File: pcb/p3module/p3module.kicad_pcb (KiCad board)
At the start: 2 copper layers, 38 parts, among them J1 Conn_01x08_Female, J2 Conn_02x10_Counter_Clockwise, J3 Conn_01x08_Female, U1 74HC595, U2 74HC165, U3 74HC595, U4 4051

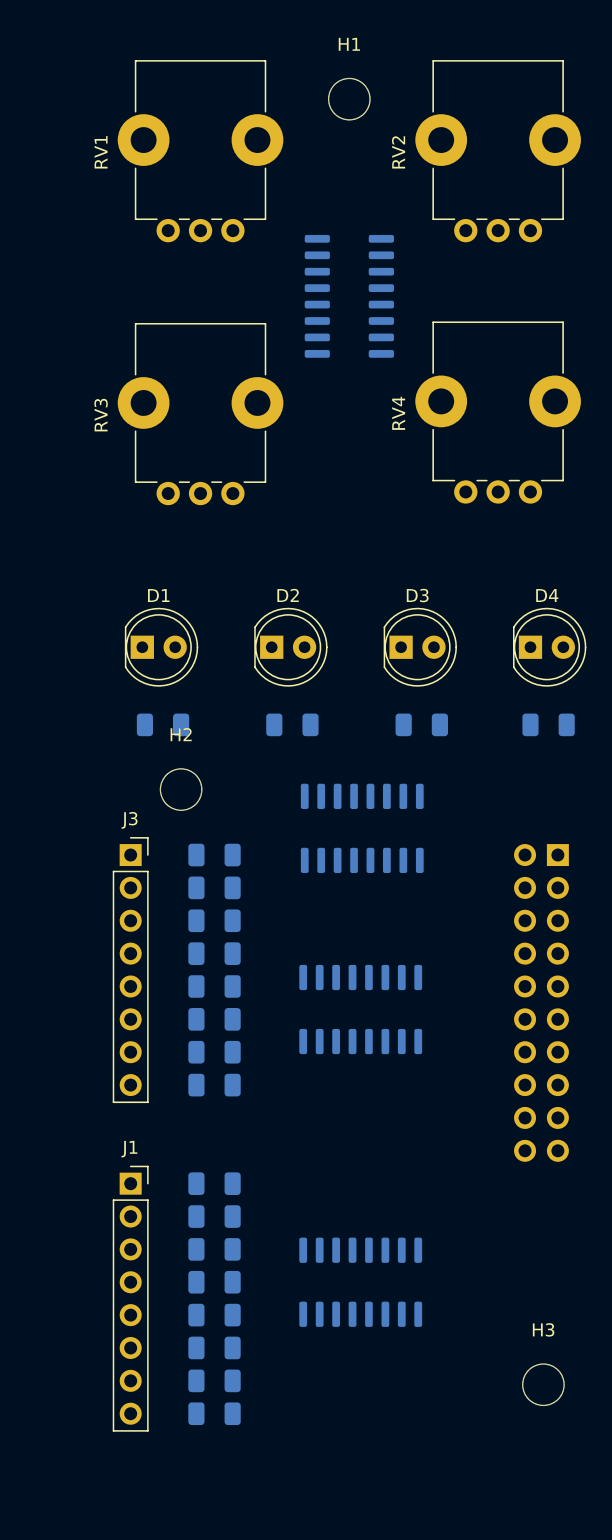
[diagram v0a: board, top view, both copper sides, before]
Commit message: reduced width to 6HP
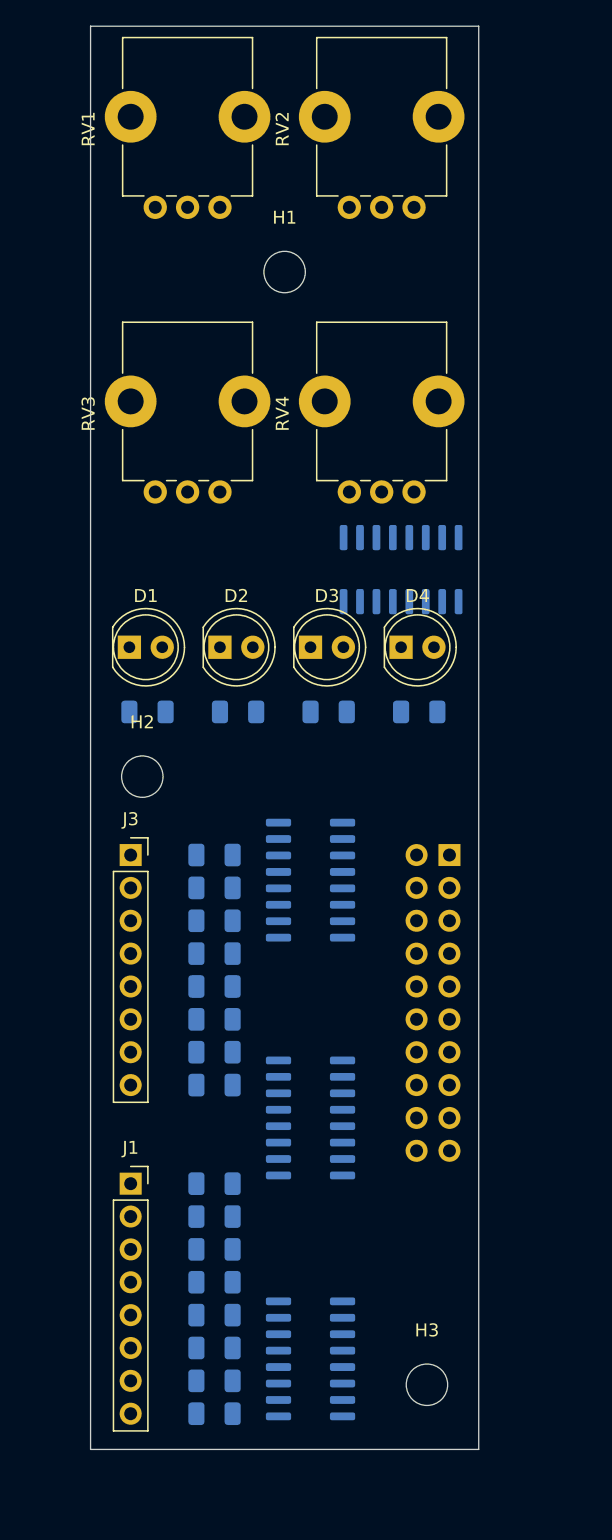
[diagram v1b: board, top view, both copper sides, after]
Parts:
- moved U4 21.5 mm to (59.0, 77.0), turned to 270 degrees
- moved H1 14.3 mm to (50.0, 54.0)
- moved R20 10.0 mm to (60.4, 88.0)
- moved D4 10.0 mm to (59.0, 83.0)
- moved U2 9.23 mm to (52.0, 119.4), turned to 180 degrees
- moved RV2 9.18 mm to (60.0, 49.0)
- moved H3 9.00 mm to (61.0, 140.0)
- moved RV4 9.00 mm to (60.0, 71.0)
- moved J2 8.38 mm to (62.7, 99.1)
- moved R19 7.27 mm to (53.4, 88.0)
- moved U1 7.08 mm to (52.0, 138.0), turned to 180 degrees
- moved D3 7.00 mm to (52.0, 83.0)
- moved U3 5.66 mm to (52.0, 101.0), turned to 180 degrees
- moved R18 4.32 mm to (46.4, 88.0)
- moved D2 4.00 mm to (45.0, 83.0)
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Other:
- board outline added: 30 x 110 mm

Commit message: reduced height to 10cm
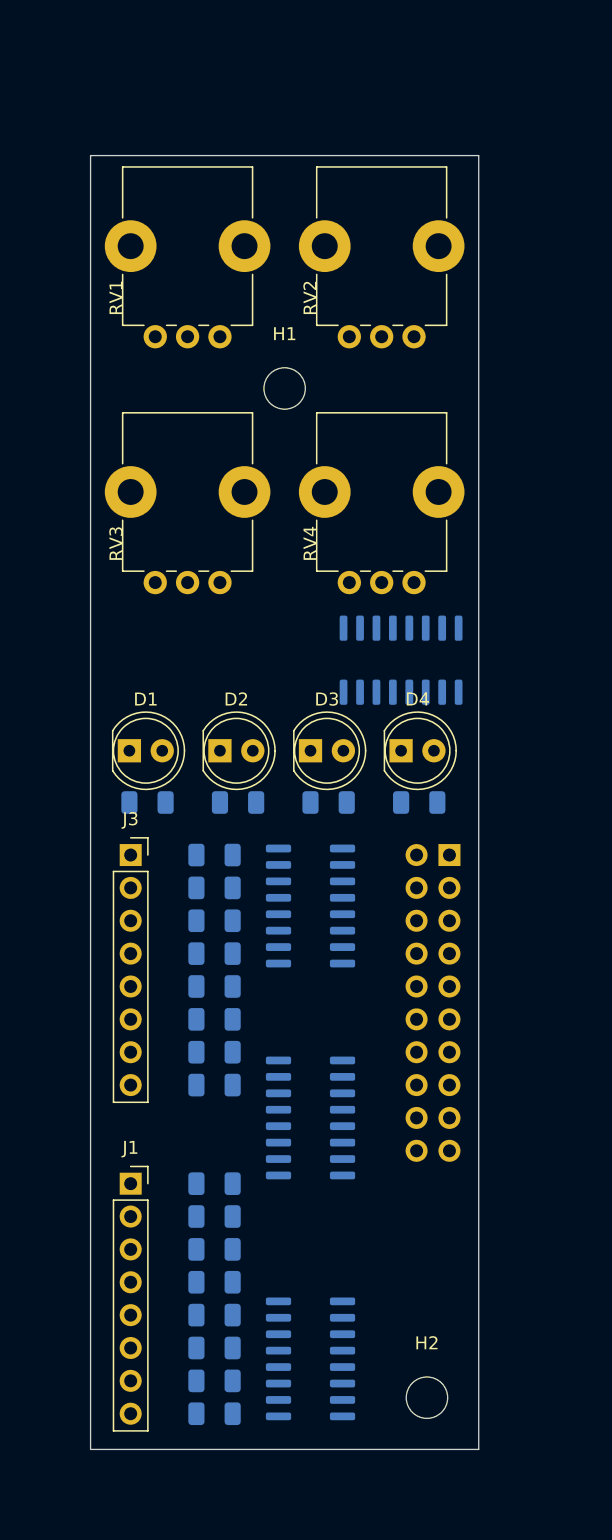
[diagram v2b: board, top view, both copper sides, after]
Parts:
- removed H3: MountingHole, MountingHole:MountingHole_3.2mm_M3
- moved H2 52.8 mm to (61.0, 141.0)
- moved RV1 10.0 mm to (45.0, 59.0)
- moved RV2 10.0 mm to (60.0, 59.0)
- moved H1 9.00 mm to (50.0, 63.0)
- moved D1 8.00 mm to (38.0, 91.0)
- moved D2 8.00 mm to (45.0, 91.0)
- moved D3 8.00 mm to (52.0, 91.0)
- moved D4 8.00 mm to (59.0, 91.0)
- moved R17 7.00 mm to (39.4, 95.0)
- moved R18 7.00 mm to (46.4, 95.0)
- moved R19 7.00 mm to (53.4, 95.0)
- moved R20 7.00 mm to (60.4, 95.0)
- moved RV3 7.00 mm to (45.0, 78.0)
- moved RV4 7.00 mm to (60.0, 78.0)
- moved U4 7.00 mm to (59.0, 84.0)
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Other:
- board size 30 x 110 mm -> 30 x 100 mm
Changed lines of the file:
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@@
   (general
     (thickness 1.6)
-    (drawings 8)
+    (drawings 4)
     (tracks 0)
     (zones 0)
-    (modules 38)
+    (modules 37)
     (nets 66)
   )
@@
   )
   (module Package_SO:SOIC-16_3.9x9.9mm_P1.27mm (layer B.Cu)
-    (at 59 77 270)
+    (at 59 84 270)
     (descr "SOIC, 16 Pin (JEDEC MS-012AC, https://www.analog.com/media/en/package-pcb-resources/package/pkg_pdf/soic_narrow-r/r_16.pdf), generated with kicad-footprint-generator ipc_gullwing_generator.py")
     (tags "SOIC SO")
@@
   )
   (module Package_SO:SOIC-16_3.9x9.9mm_P1.27mm (layer B.Cu)
-    (at 52 101 180)
+    (at 52 103 180)
     (descr "SOIC, 16 Pin (JEDEC MS-012AC, https://www.analog.com/media/en/package-pcb-resources/package/pkg_pdf/soic_narrow-r/r_16.pdf), generated with kicad-footprint-generator ipc_gullwing_generator.py")
     (tags "SOIC SO")
@@
   )
   (module Resistor_SMD:R_1206_3216Metric (layer B.Cu)
-    (at 60.4 88 180)
+    (at 60.4 95 180)
     (descr "Resistor SMD 1206 (3216 Metric), square (rectangular) end terminal, IPC_7351 nominal, (Body size source: http://www.tortai-tech.com/upload/download/2011102023233369053.pdf), generated with kicad-footprint-generator")
     (tags resistor)
@@
   )
   (module Resistor_SMD:R_1206_3216Metric (layer B.Cu)
-    (at 53.4 88 180)
+    (at 53.4 95 180)
     (descr "Resistor SMD 1206 (3216 Metric), square (rectangular) end terminal, IPC_7351 nominal, (Body size source: http://www.tortai-tech.com/upload/download/2011102023233369053.pdf), generated with kicad-footprint-generator")
     (tags resistor)
@@
   )
   (module Resistor_SMD:R_1206_3216Metric (layer B.Cu)
-    (at 46.4 88 180)
+    (at 46.4 95 180)
     (descr "Resistor SMD 1206 (3216 Metric), square (rectangular) end terminal, IPC_7351 nominal, (Body size source: http://www.tortai-tech.com/upload/download/2011102023233369053.pdf), generated with kicad-footprint-generator")
     (tags resistor)
@@
   )
   (module Resistor_SMD:R_1206_3216Metric (layer B.Cu)
-    (at 39.4 88 180)
+    (at 39.4 95 180)
     (descr "Resistor SMD 1206 (3216 Metric), square (rectangular) end terminal, IPC_7351 nominal, (Body size source: http://www.tortai-tech.com/upload/download/2011102023233369053.pdf), generated with kicad-footprint-generator")
     (tags resistor)
@@
   )
   (module Potentiometer_THT:Potentiometer_Alps_RK09K_Single_Vertical (layer F.Cu)
-    (at 60 71 90)
+    (at 60 78 90)
     (descr "Potentiometer, vertical, Alps RK09K Single, http://www.alps.com/prod/info/E/HTML/Potentiometer/RotaryPotentiometers/RK09K/RK09K_list.html")
     (tags "Potentiometer vertical Alps RK09K Single")
-    (fp_text reference RV4 (at 6.05 -10.15 90) (layer F.SilkS)
+    (fp_text reference RV4 (at 3 -8 90) (layer F.SilkS)
       (effects (font (size 1 1) (thickness 0.15)))
     )
@@
   )
   (module Potentiometer_THT:Potentiometer_Alps_RK09K_Single_Vertical (layer F.Cu)
-    (at 45 71 90)
+    (at 45 78 90)
     (descr "Potentiometer, vertical, Alps RK09K Single, http://www.alps.com/prod/info/E/HTML/Potentiometer/RotaryPotentiometers/RK09K/RK09K_list.html")
     (tags "Potentiometer vertical Alps RK09K Single")
-    (fp_text reference RV3 (at 6.05 -10.15 90) (layer F.SilkS)
+    (fp_text reference RV3 (at 3 -8 90) (layer F.SilkS)
       (effects (font (size 1 1) (thickness 0.15)))
     )
@@
   )
   (module Potentiometer_THT:Potentiometer_Alps_RK09K_Single_Vertical (layer F.Cu)
-    (at 60 49 90)
+    (at 60 59 90)
     (descr "Potentiometer, vertical, Alps RK09K Single, http://www.alps.com/prod/info/E/HTML/Potentiometer/RotaryPotentiometers/RK09K/RK09K_list.html")
     (tags "Potentiometer vertical Alps RK09K Single")
-    (fp_text reference RV2 (at 6.05 -10.15 90) (layer F.SilkS)
+    (fp_text reference RV2 (at 3 -8 90) (layer F.SilkS)
       (effects (font (size 1 1) (thickness 0.15)))
     )
@@
   )
   (module Potentiometer_THT:Potentiometer_Alps_RK09K_Single_Vertical (layer F.Cu)
-    (at 45 49 90)
+    (at 45 59 90)
     (descr "Potentiometer, vertical, Alps RK09K Single, http://www.alps.com/prod/info/E/HTML/Potentiometer/RotaryPotentiometers/RK09K/RK09K_list.html")
     (tags "Potentiometer vertical Alps RK09K Single")
-    (fp_text reference RV1 (at 6.05 -10.15 90) (layer F.SilkS)
+    (fp_text reference RV1 (at 3 -8 90) (layer F.SilkS)
       (effects (font (size 1 1) (thickness 0.15)))
     )
@@
   )
   (module MountingHole:MountingHole_3.2mm_M3 (layer F.Cu)
-    (at 61 140)
-    (descr "Mounting Hole 3.2mm, no annular, M3")
-    (tags "mounting hole 3.2mm no annular m3")
-    (attr virtual)
-    (fp_text reference H3 (at 0 -4.2) (layer F.SilkS)
-      (effects (font (size 1 1) (thickness 0.15)))
-    )
-    (fp_text value MountingHole (at 0 4.2) (layer F.Fab)
-      (effects (font (size 1 1) (thickness 0.15)))
-    )
-    (fp_text user %R (at 0.3 0) (layer F.Fab)
-      (effects (font (size 1 1) (thickness 0.15)))
-    )
-    (fp_circle (center 0 0) (end 3.2 0) (layer Cmts.User) (width 0.15))
-    (fp_circle (center 0 0) (end 3.45 0) (layer F.CrtYd) (width 0.05))
-    (pad 1 np_thru_hole circle (at 0 0) (size 3.2 3.2) (drill 3.2) (layers *.Cu *.Mask))
-  )
-  (module MountingHole:MountingHole_3.2mm_M3 (layer F.Cu)
-    (at 39 93)
+    (at 61 141)
     (descr "Mounting Hole 3.2mm, no annular, M3")
     (tags "mounting hole 3.2mm no annular m3")
@@
   )
   (module MountingHole:MountingHole_3.2mm_M3 (layer F.Cu)
-    (at 50 54)
+    (at 50 63)
     (descr "Mounting Hole 3.2mm, no annular, M3")
     (tags "mounting hole 3.2mm no annular m3")
@@
   )
   (module LED_THT:LED_D5.0mm (layer F.Cu)
-    (at 59 83)
+    (at 59 91)
     (descr "LED, diameter 5.0mm, 2 pins, http://cdn-reichelt.de/documents/datenblatt/A500/LL-504BC2E-009.pdf")
     (tags "LED diameter 5.0mm 2 pins")
@@
   )
   (module LED_THT:LED_D5.0mm (layer F.Cu)
-    (at 52 83)
+    (at 52 91)
     (descr "LED, diameter 5.0mm, 2 pins, http://cdn-reichelt.de/documents/datenblatt/A500/LL-504BC2E-009.pdf")
     (tags "LED diameter 5.0mm 2 pins")
@@
   )
   (module LED_THT:LED_D5.0mm (layer F.Cu)
-    (at 45 83)
+    (at 45 91)
     (descr "LED, diameter 5.0mm, 2 pins, http://cdn-reichelt.de/documents/datenblatt/A500/LL-504BC2E-009.pdf")
     (tags "LED diameter 5.0mm 2 pins")
@@
   )
   (module LED_THT:LED_D5.0mm (layer F.Cu)
-    (at 38 83)
+    (at 38 91)
     (descr "LED, diameter 5.0mm, 2 pins, http://cdn-reichelt.de/documents/datenblatt/A500/LL-504BC2E-009.pdf")
     (tags "LED diameter 5.0mm 2 pins")
@@
     )
   )
-  (gr_line (start 35 145) (end 35 35) (layer Edge.Cuts) (width 0.05))
+  (gr_line (start 35 45) (end 65 45) (layer Edge.Cuts) (width 0.05))
+  (gr_line (start 35 145) (end 35 45) (layer Edge.Cuts) (width 0.05))
   (gr_line (start 65 145) (end 35 145) (layer Edge.Cuts) (width 0.05))
-  (gr_line (start 65 35) (end 65 145) (layer Edge.Cuts) (width 0.05))
-  (gr_line (start 35 35) (end 65 35) (layer Edge.Cuts) (width 0.05))
-  (gr_line (start 35 145) (end 65 145) (layer Dwgs.User) (width 0.15))
-  (gr_line (start 35 35) (end 65 35) (layer Dwgs.User) (width 0.15))
-  (gr_line (start 65 35) (end 65 145) (layer Dwgs.User) (width 0.15))
-  (gr_line (start 35 145) (end 35 35) (layer Dwgs.User) (width 0.15))
+  (gr_line (start 65 45) (end 65 145) (layer Edge.Cuts) (width 0.05))
 )

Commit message: routing is hard
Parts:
- moved U3 21.0 mm to (43.0, 84.0), turned to 270 degrees
- moved U2 11.7 mm to (52.6, 107.7)
- moved U1 4.65 mm to (52.0, 133.3), turned to 0 degrees
- moved R1 2.54 mm to (42.0, 124.5)
- moved R2 2.54 mm to (42.0, 127.0)
- moved R3 2.54 mm to (42.0, 129.5)
- moved R4 2.54 mm to (42.0, 132.1)
- moved R5 2.54 mm to (42.0, 134.6)
- moved R6 2.54 mm to (42.0, 137.2)
- moved R7 2.54 mm to (42.0, 139.7)
- moved R8 2.54 mm to (42.0, 142.2)
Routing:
- net VCC: track 0.00 -> 211.3 mm, vias 0 -> 1
- net /OUT_DATA_IN: track 0.00 -> 44.8 mm, vias 0 -> 1
- net /POT2: track 0.00 -> 43.4 mm, vias 0 -> 2
- net /OUT_LATCH: track 0.00 -> 39.3 mm, vias 0 -> 1
- net /OUT_CLOCK: track 0.00 -> 39.1 mm, vias 0 -> 2
- net /OUT_DATA_OUT: track 0.00 -> 36.9 mm
- net /POT1: track 0.00 -> 35.9 mm, vias 0 -> 2
- net Net-(R8-Pad2): track 0.00 -> 30.1 mm
- net Net-(R18-Pad2): track 0.00 -> 24.7 mm
- net Net-(R20-Pad2): track 0.00 -> 24.3 mm, vias 0 -> 2
- net Net-(J3-Pad2): track 0.00 -> 21.7 mm
- net Net-(J3-Pad8): track 0.00 -> 21.0 mm
- net Net-(J3-Pad7): track 0.00 -> 19.4 mm
- net Net-(J3-Pad5): track 0.00 -> 19.1 mm
- net Net-(R19-Pad2): track 0.00 -> 19.1 mm, vias 0 -> 2
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- added copper zone on B.Cu, net GND
- added copper zone on F.Cu, net GND

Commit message: another attempt at routing
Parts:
- J2: value Conn_02x10_Counter_Clockwise -> Conn_02x10_Odd_Even; moved to F.Cu
- moved J2 28.0 mm to (61.0, 127.0)
- moved U2 2.79 mm to (51.0, 110.0), turned to 90 degrees
- moved R10 2.54 mm to (42.0, 101.6)
- moved R11 2.54 mm to (42.0, 104.1)
- moved R12 2.54 mm to (42.0, 106.7)
- moved R13 2.54 mm to (42.0, 109.2)
- moved R14 2.54 mm to (42.0, 111.8)
- moved R15 2.54 mm to (42.0, 114.3)
- moved R16 2.54 mm to (42.0, 116.8)
- moved R9 2.54 mm to (42.0, 99.1)
- moved U1 1.19 mm to (51.0, 134.0), turned to 90 degrees
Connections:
- J2 pad 10: GND -> /ANA_CHAN1
- J2 pad 11: /LED_DATA_IN -> /IN_LOAD
- J2 pad 12: /LED_CLOCK -> /ANA_CHAN0
- J2 pad 13: /LED_LATCH -> /IN_CLOCK
- J2 pad 15: /ANA_CHAN0 -> /IN_CLOCK_ENABLE
- J2 pad 16: /ANA_CHAN1 -> /LED_LATCH
- J2 pad 17: /ANA_CHAN2 -> /IN_DATA_IN
- J2 pad 18: /ANA_OUT -> /LED_CLOCK
- J2 pad 19: Net-(J2-Pad19) -> GND
- J2 pad 2: /OUT_CLOCK -> VCC
- J2 pad 20: VCC -> /LED_DATA_IN
- J2 pad 3: /OUT_LATCH -> /OUT_CLOCK
- J2 pad 4: /OUT_DATA_OUT -> Net-(J2-Pad4)
- J2 pad 5: /IN_DATA_OUT -> /OUT_LATCH
- J2 pad 6: /IN_LOAD -> /ANA_OUT
- J2 pad 7: /IN_CLOCK -> /OUT_DATA_OUT
- J2 pad 8: /IN_CLOCK_ENABLE -> /ANA_CHAN2
- J2 pad 9: /IN_DATA_IN -> /IN_DATA_OUT
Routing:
- net VCC: track 211.3 -> 0.00 mm, vias 1 -> 0
- net /OUT_DATA_IN: track 44.8 -> 0.00 mm, vias 1 -> 0
- net /POT2: track 43.4 -> 0.00 mm, vias 2 -> 0
- net /OUT_LATCH: track 39.3 -> 0.00 mm, vias 1 -> 0
- net /OUT_CLOCK: track 39.1 -> 0.00 mm, vias 2 -> 0
- net /OUT_DATA_OUT: track 36.9 -> 0.00 mm
- net /POT1: track 35.9 -> 0.00 mm, vias 2 -> 0
- net Net-(R8-Pad2): track 30.1 -> 0.00 mm
- net Net-(R18-Pad2): track 24.7 -> 0.00 mm
- net Net-(R20-Pad2): track 24.3 -> 0.00 mm, vias 2 -> 0
- net Net-(J3-Pad2): track 21.7 -> 0.00 mm
- net Net-(J3-Pad8): track 21.0 -> 0.00 mm
- net Net-(J3-Pad7): track 19.4 -> 0.00 mm
- net Net-(J3-Pad5): track 19.1 -> 0.00 mm
- net Net-(R19-Pad2): track 19.1 -> 0.00 mm, vias 2 -> 0
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
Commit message: slightly better routing
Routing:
- net VCC: track 0.00 -> 206.2 mm, vias 0 -> 4
- net /POT1: track 0.00 -> 48.5 mm, vias 0 -> 1
- net /ANA_OUT: track 0.00 -> 45.1 mm, vias 0 -> 1
- net Net-(R1-Pad2): track 0.00 -> 43.1 mm
- net /ANA_CHAN2: track 0.00 -> 38.5 mm
- net /LED_LATCH: track 0.00 -> 37.6 mm
- net Net-(J3-Pad4): track 0.00 -> 36.0 mm
- net /ANA_CHAN1: track 0.00 -> 35.9 mm
- net /LED_DATA_OUT: track 0.00 -> 33.9 mm, vias 0 -> 1
- net Net-(R2-Pad2): track 0.00 -> 33.0 mm
- net Net-(J3-Pad5): track 0.00 -> 32.9 mm
- net /LED_CLOCK: track 0.00 -> 31.5 mm
- net Net-(J3-Pad3): track 0.00 -> 31.4 mm
- net /ANA_CHAN0: track 0.00 -> 31.4 mm
- net /POT2: track 0.00 -> 30.4 mm, vias 0 -> 1
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
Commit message: routing worked but one of the sockets was on the wrong side. ugh
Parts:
- moved H1 1.00 mm to (50.0, 62.0)
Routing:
- net GND: track 20.9 -> 26.9 mm, vias 1 -> 8
- net /POT2: track 30.4 -> 32.9 mm, vias 1 -> 2

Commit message: better routing
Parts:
- J2: moved to B.Cu
- moved U4 2.83 mm to (57.0, 86.0)
- moved R10 2.54 mm to (42.0, 104.1)
- moved R11 2.54 mm to (42.0, 106.7)
- moved R13 2.54 mm to (42.0, 111.8)
- moved R15 2.54 mm to (42.0, 116.8)
- moved J3 2.54 mm to (38.1, 101.6)
- moved R12 2.54 mm to (42.0, 109.2)
- moved R14 2.54 mm to (42.0, 114.3)
- moved R16 2.54 mm to (42.0, 119.4)
- moved R9 2.54 mm to (42.0, 101.6)
- moved D1 2.00 mm to (38.0, 93.0)
- moved D2 2.00 mm to (45.0, 93.0)
- moved D3 2.00 mm to (52.0, 93.0)
- moved D4 2.00 mm to (59.0, 93.0)
- moved R17 2.00 mm to (39.4, 97.0)
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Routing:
- net GND: track 26.9 -> 67.2 mm, vias 8 -> 7
- net Net-(R1-Pad2): track 43.1 -> 18.6 mm
- net Net-(R2-Pad2): track 33.0 -> 18.7 mm
- net VCC: track 206.2 -> 195.1 mm, vias 4 -> 6
- net /POT1: track 48.5 -> 40.6 mm
- net Net-(J3-Pad4): track 36.0 -> 43.6 mm
- net /ANA_CHAN1: track 35.9 -> 28.5 mm, vias 0 -> 1
- net Net-(R7-Pad2): track 7.21 -> 14.6 mm
- net Net-(R18-Pad2): track 17.5 -> 24.7 mm
- net /IN_DATA_IN: track 21.0 -> 14.8 mm
- net Net-(R8-Pad2): track 13.4 -> 7.58 mm
- net Net-(R20-Pad2): track 24.4 -> 29.5 mm, vias 2 -> 0
- net /LED_LATCH: track 37.6 -> 33.1 mm
- net /OUT_LATCH: track 22.4 -> 18.1 mm
- net /ANA_OUT: track 45.1 -> 41.1 mm
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
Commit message: done for the day
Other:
- board text added: "1"
- board text added: "2"
- board text added: "3"
- board text added: "4"
- board text added: "GND"
- board text added: "INPUT 0 INPUT 1 INPUT 2 INPUT 3 INPUT 4 INPUT 5 INPUT 6 INPUT 7"
- board text added: "OUTPUT 0 OUTPUT 1 OUTPUT 2 OUTPUT 3 OUTPUT 4 OUTPUT 5 OUTPUT 6 OUTPUT 7"
- board text added: "VCC"
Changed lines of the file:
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@@
   (general
     (thickness 1.6)
-    (drawings 4)
+    (drawings 12)
     (tracks 363)
     (zones 0)
@@
     (descr "Through hole straight pin header, 2x10, 2.54mm pitch, double rows")
     (tags "Through hole pin header THT 2x10 2.54mm double row")
-    (fp_text reference J2 (at 1.27 2.33) (layer B.SilkS)
+    (fp_text reference J2 (at -1 2.33) (layer B.SilkS)
       (effects (font (size 1 1) (thickness 0.15)) (justify mirror))
     )
@@
     )
   )
+  (gr_text VCC (at 63 127.58 90) (layer B.SilkS)
+    (effects (font (size 1 1) (thickness 0.15)) (justify left mirror))
+  )
+  (gr_text GND (at 58.42 103) (layer B.SilkS)
+    (effects (font (size 1 1) (thickness 0.15)) (justify left mirror))
+  )
+  (gr_text 3 (at 42.5 84) (layer F.SilkS)
+    (effects (font (size 3 3) (thickness 0.15)))
+  )
+  (gr_text 4 (at 57.5 84) (layer F.SilkS)
+    (effects (font (size 3 3) (thickness 0.15)))
+  )
+  (gr_text 2 (at 57.5 63) (layer F.SilkS)
+    (effects (font (size 3 3) (thickness 0.15)))
+  )
+  (gr_text 1 (at 42.5 63) (layer F.SilkS)
+    (effects (font (size 3 3) (thickness 0.15)))
+  )
+  (gr_text "OUTPUT 0\nOUTPUT 1\nOUTPUT 2\nOUTPUT 3\nOUTPUT 4\nOUTPUT 5\nOUTPUT 6\nOUTPUT 7" (at 40.64 133.35) (layer F.SilkS)
+    (effects (font (size 1.6 1.6) (thickness 0.15)) (justify left))
+  )
+  (gr_text "INPUT 0\nINPUT 1\nINPUT 2\nINPUT 3\nINPUT 4\nINPUT 5\nINPUT 6\nINPUT 7" (at 40.64 110.49) (layer F.SilkS)
+    (effects (font (size 1.6 1.6) (thickness 0.15)) (justify left))
+  )
   (gr_line (start 35 45) (end 65 45) (layer Edge.Cuts) (width 0.05))
